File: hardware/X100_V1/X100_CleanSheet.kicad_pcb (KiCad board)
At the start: 4 copper layers, 45 x 45 mm, 205 parts, among them J401 USB4105-GF-A, J501 1040310811, J601 SM04B-GHS-TB(LF)(SN), J701 SM06B-GHS-TB(LF)(SN), J702 SM06B-GHS-TB(LF)(SN), J703 SM06B-GHS-TB(LF)(SN), J704 SM04B-GHS-TB(LF)(SN), J801 OUT1 /GND, J802 OUT2 /GND, J803 OUT3 /GND, J804 OUT4 /GND, J805 OUT5 /GND, J806 OUT6 /GND, J807 SWD:1REF2GND3IO4CLK5NRST, J808 BATTERY/bench3S-6S ONLY, J809 CURRENT monitor only, Q101 DMP6023LSS-13, U101 TPS54360BDDAR, U102 AP63203WU-7, U103 TPS7A2033PDBVR, U104 TPS2553DBVR, U201 STM32H743VIT6, U301 BMI088, U302 SPL06-001, U401 TPD2E2U06QDBZRQ1, U402 SN74LVC1G17DBVR, U403 TPD2E2U06QDBZRQ1, U404 TPD2E2U06QDBZRQ1, U601 TCAN3414DR, U801 TMUX1511PWR, Y201 8.000MHz /CL20pF

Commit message: fix(pcb): close J601 clearance and stage unapproved J401 review
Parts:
- JP601, R204, TP809: moved to B.Cu
- moved J802 26.4 mm to (79.0, 82.0), turned to 90 degrees
- moved J801 20.7 mm to (79.8, 79.0), turned to 90 degrees
- moved R602 10.2 mm to (89.7, 82.2)
- moved TP710 9.13 mm to (95.5, 79.0)
- moved J701 8.45 mm to (100.1, 80.7)
- moved TP603 7.85 mm to (90.2, 79.0)
- moved J601 7.57 mm to (89.3, 80.7)
- moved JP601 7.21 mm to (85.9, 81.5)
- moved TP703 6.65 mm to (88.5, 79.0)
- moved R204 6.36 mm to (104.0, 79.9), turned to 0 degrees
- moved TP605 6.20 mm to (85.0, 79.0)
- moved TP708 5.99 mm to (93.8, 78.9)
- moved TP809 3.66 mm to (106.5, 79.0)
- moved TP707 3.50 mm to (92.0, 78.9)
- moved TP604 3.25 mm to (86.8, 79.0)

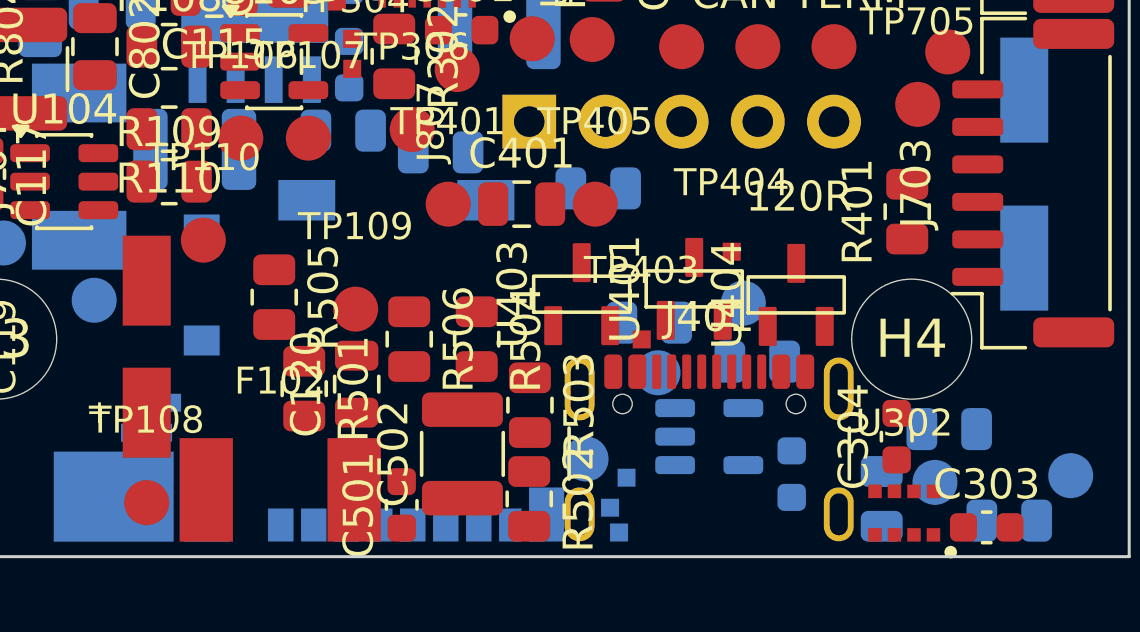
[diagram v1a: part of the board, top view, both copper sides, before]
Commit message: fix(pcb): apply approved Amphenol J401 with native netlist sync
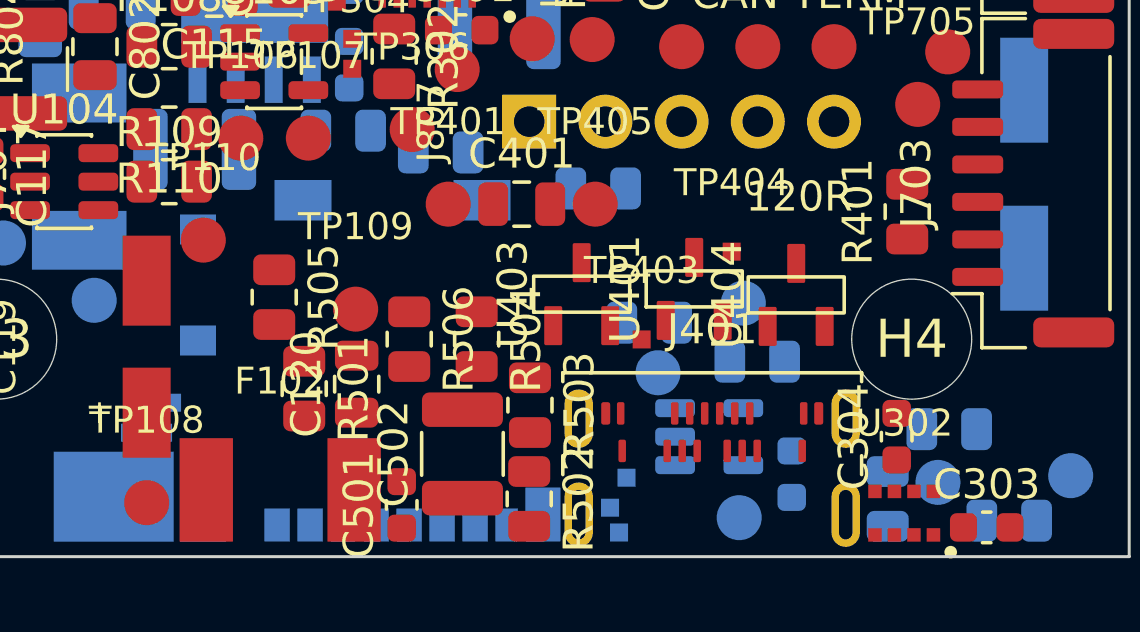
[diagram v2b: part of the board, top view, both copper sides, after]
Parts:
- J401: value USB4105-GF-A -> 124019772112A; footprint X100_Physical:Official_Connector_USB_USB_C_Receptacle_GCT_USB4105-xx-A_16P_TopMnt_Horizontal -> X100_Physical:Official_USB_C_Amphenol_124019772112A
- moved TP501 5.47 mm to (109.5, 121.2)
- moved J401 0.92 mm to (108.6, 120.9)
- moved R303 0.20 mm to (114.5, 120.6)
- moved J501 0.12 mm to (97.2, 116.0)
- moved TP307 0.10 mm to (116.1, 120.0)

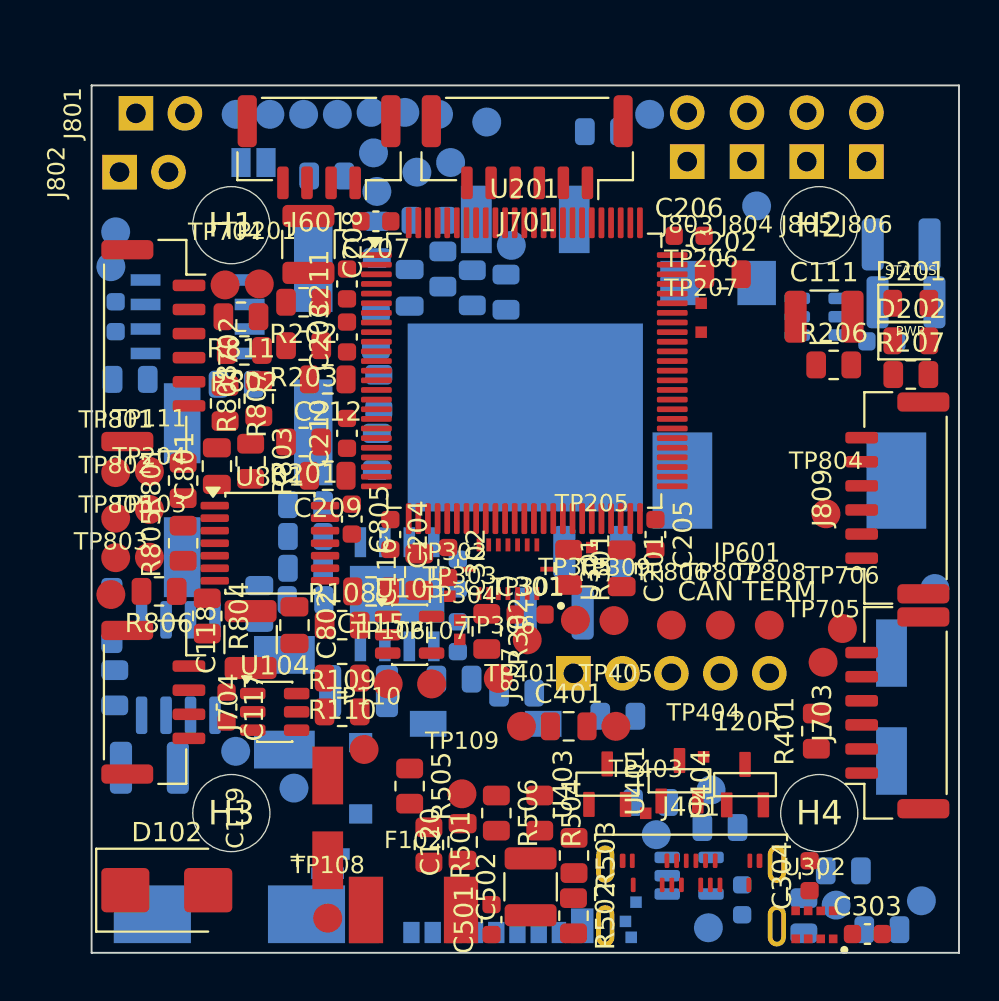
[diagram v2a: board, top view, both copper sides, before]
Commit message: fix(pcb): improve testpoint clearance and synchronize schematic fields
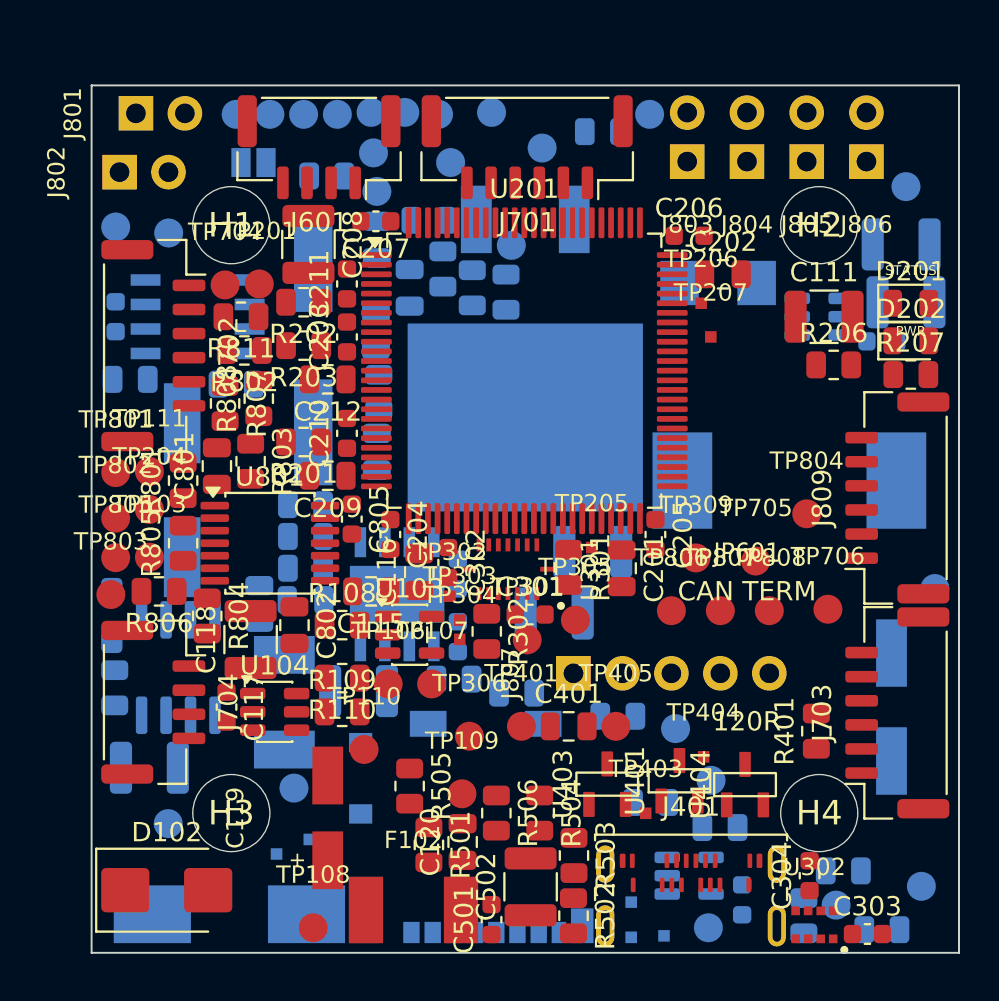
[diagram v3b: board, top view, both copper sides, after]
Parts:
- moved TP105 7.81 mm to (119.8, 82.8)
- moved TP701 6.62 mm to (100.9, 80.8)
- moved TP705 6.31 mm to (112.0, 102.2)
- moved TP508 5.59 mm to (107.8, 110.9)
- moved TP309 5.35 mm to (108.8, 102.0)
- moved TP102 5.13 mm to (81.5, 115.8)
- moved TP506 3.50 mm to (87.1, 117.4)
- moved TP601 3.47 mm to (81.5, 85.2)
- moved TP306 3.35 mm to (97.1, 111.3)
- moved TP503 2.30 mm to (88.8, 116.6)
- moved TP504 2.14 mm to (107.2, 121.6)
- moved TP706 1.25 mm to (115.7, 104.7)
- moved TP804 1.00 mm to (114.6, 99.7)
- moved TP108 0.90 mm to (89.0, 121.2)
- moved TP308 0.75 mm to (120.5, 119.0)
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
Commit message: 紧凑测试点保留65处可测性并消除46对courtyard重叠
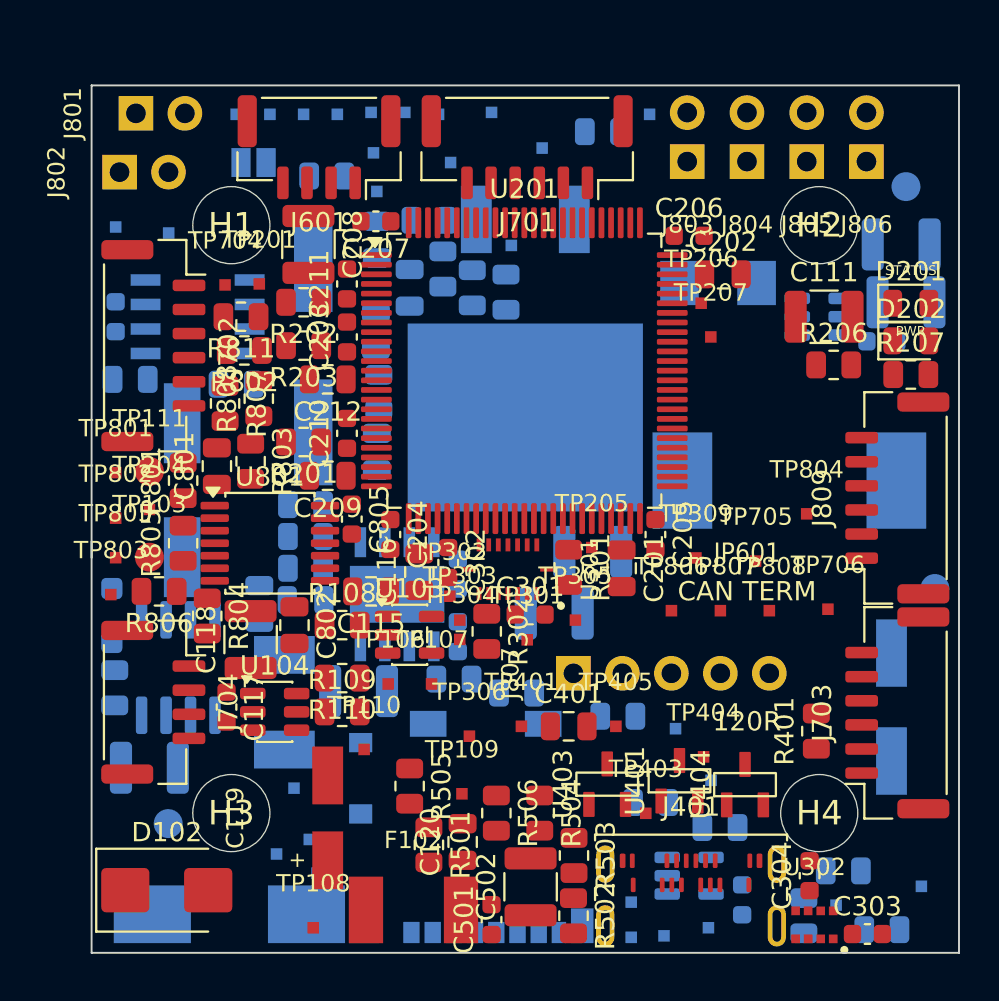
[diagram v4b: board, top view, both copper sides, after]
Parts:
- TP101, TP106, TP107, TP108, TP109, TP110, TP201, TP202, TP203, TP204, TP208, TP301, TP305, TP306, TP307, TP308, TP309, TP401, TP402, TP405, TP501, TP508, TP601, TP602, TP603, TP604, TP605, TP701, TP702, TP703, TP704, TP705, TP706, TP707, TP708, TP709, TP710, TP801, TP802, TP803, TP804, TP805, TP806, TP807, TP808, TP809: footprint X100_Physical:TP1p5_NoPaste -> X100_Physical:TP0p6_Inline_NoPaste
